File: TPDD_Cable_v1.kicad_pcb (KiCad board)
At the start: 2 copper layers, 34.6 x 11.1 mm, 5 parts, among them J1 7 x wire pads, J2 DB25_Male, Q1 DTA114EKA, Q2 DTA114EKA, Q3 DTA114EKA

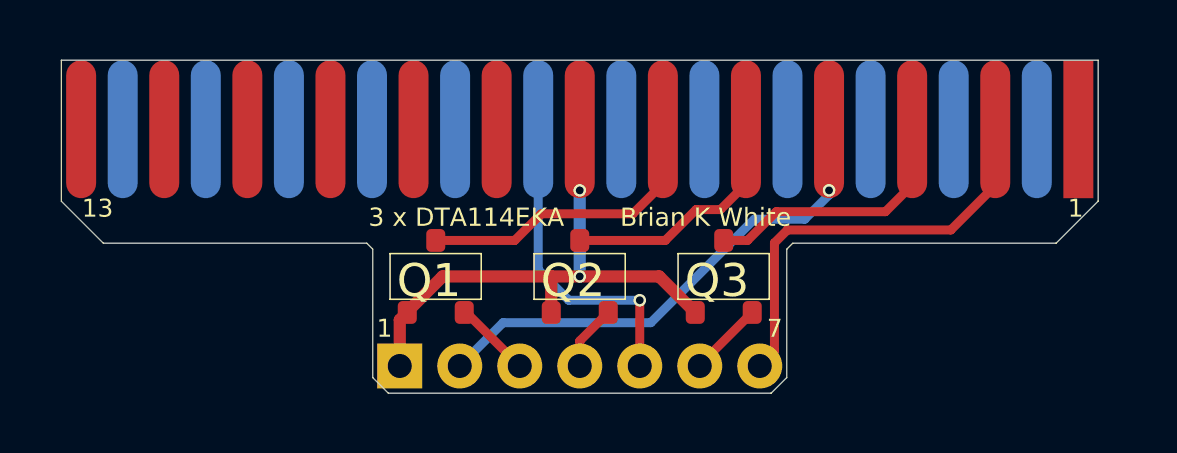
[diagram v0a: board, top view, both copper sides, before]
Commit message: pack v1 board tighter
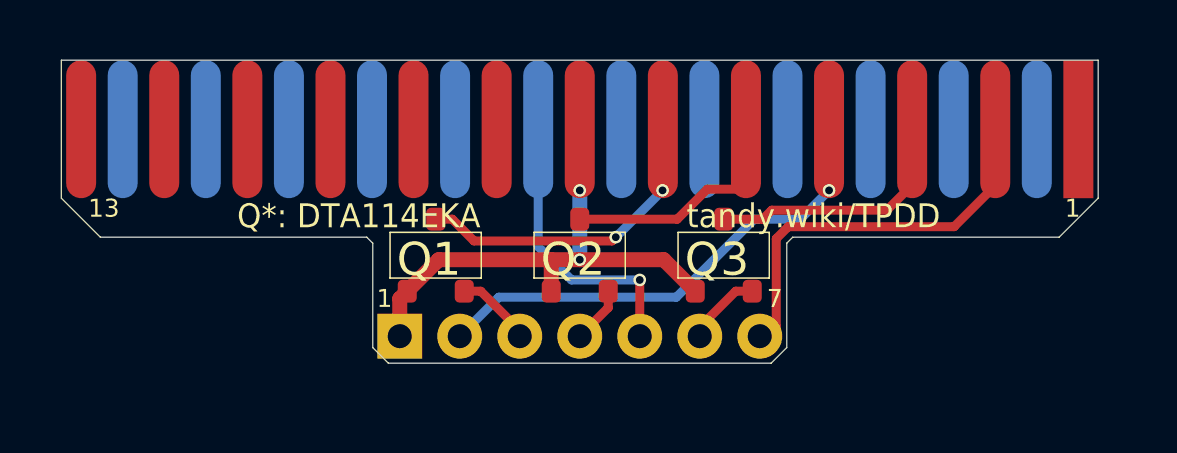
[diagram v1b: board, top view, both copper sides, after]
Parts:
- moved J1 0.99 mm to (144.9, 93.4)
- moved Q1 0.71 mm to (140.1, 90.7)
- moved Q2 0.71 mm to (144.9, 90.7)
- moved Q3 0.71 mm to (149.7, 90.7)
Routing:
- net /DSR: track 10.2 -> 8.56 mm, vias 0 -> 2
- net /GND: track 16.6 -> 15.4 mm
- net /DTR: track 10.7 -> 9.63 mm
- net /TXD: track 14.3 -> 13.8 mm
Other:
- board size 34.6 x 11.1 mm -> 34.6 x 10.1 mm
- board text added: "Q*: DTA114EKA tandy.wiki/TPDD"
- board text removed: "3 x DTA114EKA Brian K White"
- board text removed: "Tandy Portable Disk Drive"
